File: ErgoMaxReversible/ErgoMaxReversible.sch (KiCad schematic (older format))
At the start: 102 parts, among them J1 PJ-320A, K1 KEYSW, K10 KEYSW, K11 KEYSW, K12 KEYSW, K13 KEYSW, K14 KEYSW, K15 KEYSW, K16 KEYSW, K17 KEYSW, K18 KEYSW, K19 KEYSW, K2 KEYSW, K20 KEYSW, K21 KEYSW, K22 KEYSW, K23 KEYSW, K24 KEYSW, K25 KEYSW, K26 KEYSW, K27 KEYSW, K28 KEYSW, K29 KEYSW, K3 KEYSW, K30 KEYSW, K31 KEYSW, K32 KEYSW, K33 KEYSW, K34 KEYSW, K35 KEYSW, K36 KEYSW, K37 KEYSW, K38 KEYSW, K39 KEYSW, K4 KEYSW, K40 KEYSW, K41 KEYSW, K42 KEYSW, K43 KEYSW, K44 KEYSW, K5 KEYSW, K6 KEYSW, K7 KEYSW, K8 KEYSW, K9 KEYSW, U1 ProMicro

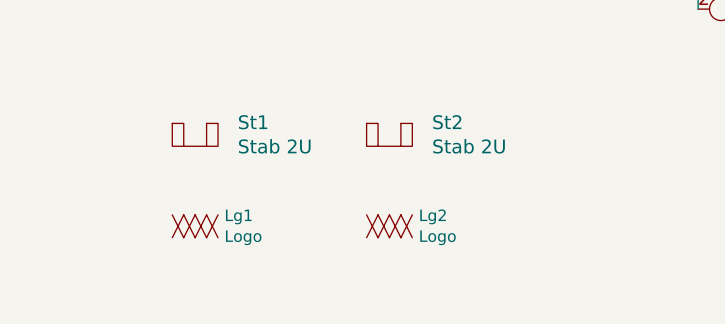
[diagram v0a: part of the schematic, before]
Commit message: update jack connector to be reversible; add logos on back of the pcb - reversible pcb
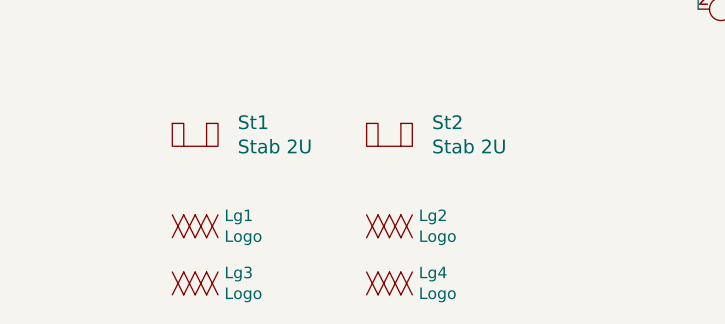
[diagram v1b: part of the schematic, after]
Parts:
- added Lg3: Logo, ErgoMax:LouWii-logo, symbol ErgoMax:Logo
- added Lg4: Logo, ErgoMax:ErgoMax-logo, symbol ErgoMax:Logo
- J1: footprint Keebio-Parts:TRRS-PJ-320A-no-Fmask -> Keebio-Parts:TRRS-PJ-320A-dual
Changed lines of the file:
@@
 EESchema Schematic File Version 4
+LIBS:ErgoMaxReversible-cache
 EELAYER 26 0
 EELAYER END
@@
 F 0 "J1" H 2600 1500 50  0000 L CNN
 F 1 "PJ-320A" H 2500 1000 50  0000 L CNN
-F 2 "Keebio-Parts:TRRS-PJ-320A-no-Fmask" H 2650 1300 50  0001 C CNN
+F 2 "Keebio-Parts:TRRS-PJ-320A-dual" H 2650 1300 50  0001 C CNN
 F 3 "~" H 2650 1300 50  0001 C CNN
 	1    2650 1300
@@
 	1    0    0    -1
 $EndComp
+$Comp
+L ErgoMax:Logo Lg3
+U 1 1 5BFED487
+P 1650 6250
+F 0 "Lg3" H 1778 6296 50  0000 L CNN
+F 1 "Logo" H 1778 6205 50  0000 L CNN
+F 2 "ErgoMax:LouWii-logo" H 1650 6150 50  0001 C CNN
+F 3 "" H 1650 6150 50  0001 C CNN
+	1    1650 6250
+	1    0    0    -1
+$EndComp
+$Comp
+L ErgoMax:Logo Lg4
+U 1 1 5C015092
+P 2500 6250
+F 0 "Lg4" H 2628 6296 50  0000 L CNN
+F 1 "Logo" H 2628 6205 50  0000 L CNN
+F 2 "ErgoMax:ErgoMax-logo" H 2500 6150 50  0001 C CNN
+F 3 "" H 2500 6150 50  0001 C CNN
+	1    2500 6250
+	1    0    0    -1
+$EndComp

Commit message: add footprints for reversible diode with and without 3d model and use it on reversible pcb
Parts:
- D1, D10, D11, D12, D13, D14, D15, D16, D17, D18, D19, D2, D20, D21, D22, D23, D24, D25, D26, D27, D28, D29, D3, D30, D31, D32, D33, D34, D35, D36, D37, D38, D39, D4, D40, D41, D42, D43, D44, D5, D6, D7, D8, D9: footprint Keebio-Parts:Diode_Long -> ErgoMax:Diode_Long_Reversible-No3dModel

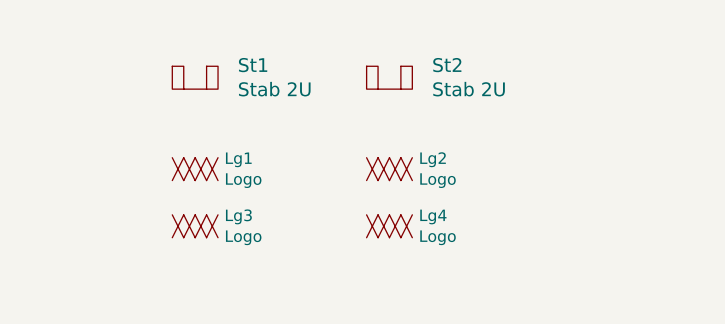
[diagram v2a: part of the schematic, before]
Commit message: improve footprints on reversible PCB and add sides markings
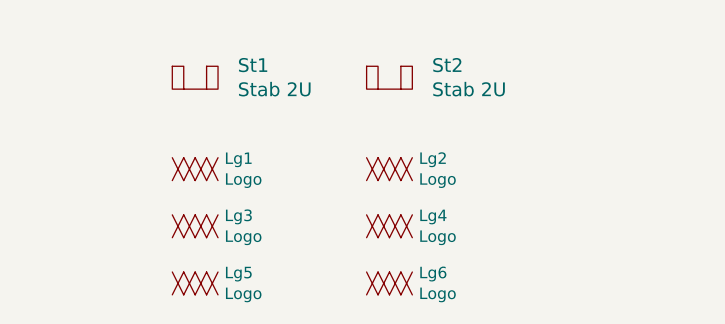
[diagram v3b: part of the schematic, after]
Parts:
- added Lg5: Logo, ErgoMax:LeftSideText, symbol ErgoMax:Logo
- added Lg6: Logo, ErgoMax:RightSideText, symbol ErgoMax:Logo
- K1, K10, K11, K12, K13, K14, K15, K16, K17, K18, K19, K2, K20, K21, K22, K23, K24, K25, K26, K27, K28, K29, K3, K30, K31, K32, K33, K34, K35, K36, K37, K38, K39, K4, K40, K41, K42, K43, K44, K5, K6, K7, K8, K9: footprint keyboard_parts:Kailh_MX_Socket_reversible -> ErgoMax:Kailh_MX_Socket_reversible

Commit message: add readme for reversible PCB
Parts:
- U1: footprint promicro:ProMicro -> ErgoMax:ProMicroReversible
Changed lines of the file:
@@
 F 0 "U1" H 1950 4437 60  0000 C CNN
 F 1 "ProMicro" H 1950 4331 60  0000 C CNN
-F 2 "promicro:ProMicro" H 2050 2350 60  0001 C CNN
+F 2 "ErgoMax:ProMicroReversible" H 2050 2350 60  0001 C CNN
 F 3 "" H 2050 2350 60  0000 C CNN
 	1    1950 3400
